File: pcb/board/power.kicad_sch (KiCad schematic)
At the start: 21 parts, among them Q1 DMG2305UX, U2 BQ25172, U3 TLV61070A, U4 XC6206P332MR

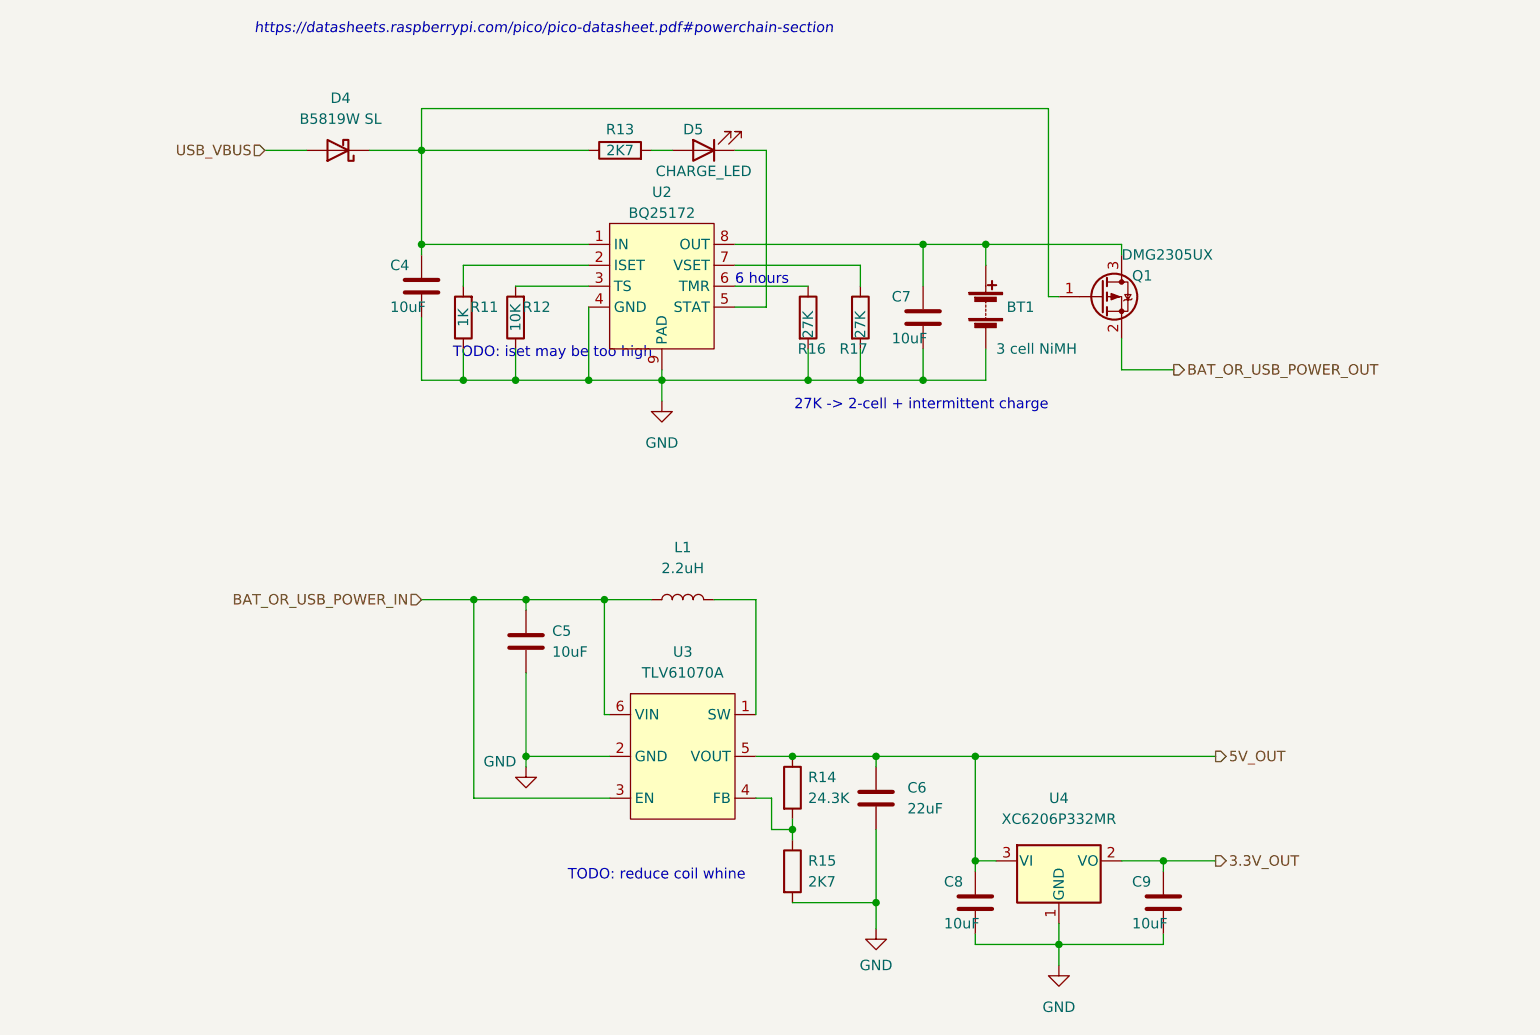
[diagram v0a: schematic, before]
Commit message: Update readmes. Uncovered I2C bug :(
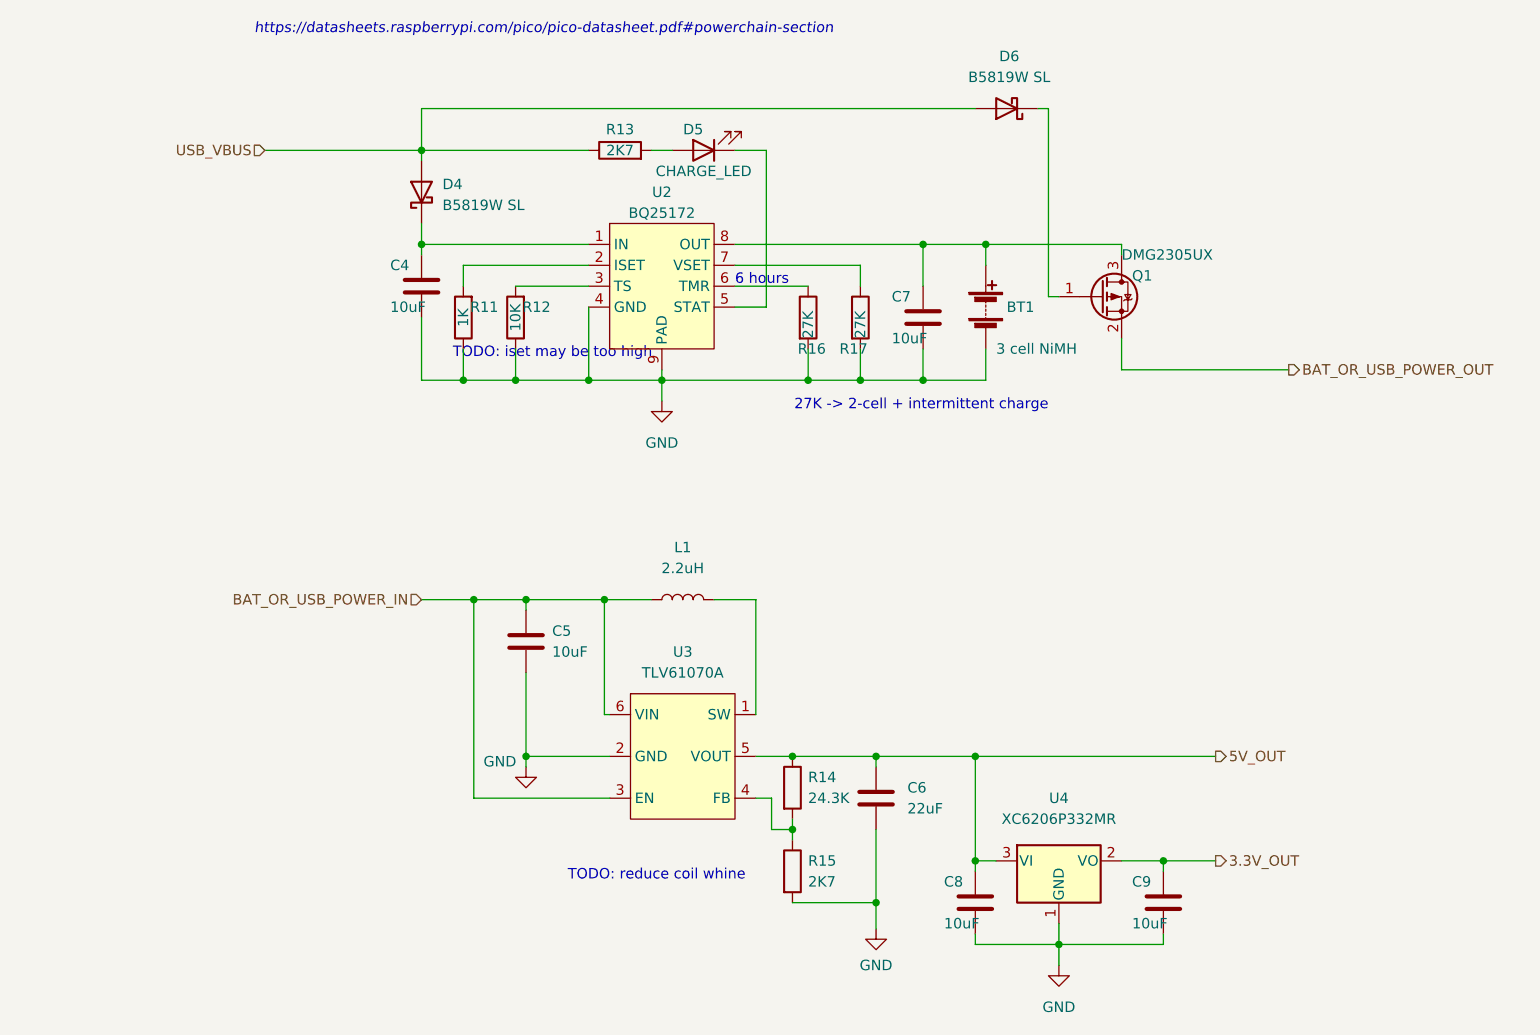
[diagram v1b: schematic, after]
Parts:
- added D6: B5819W SL, Diode_SMD:D_SOD-123, symbol Diode:1N5819
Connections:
- net USB_VBUS: now also R13.1, D6.2 (A)
- net at C4.1, D4.1 (K), U2.1 (IN): no longer Q1.1 (G), R13.1
- new net: D6.1 (K), Q1.1 (G)
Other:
- moved on the sheet: D4
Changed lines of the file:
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@@
+    (stroke (width 0) (type default) (color 0 0 0 0))
+  )
+  (wire (pts (xy 88.9 45.72) (xy 107.95 45.72))
     (stroke (width 0) (type default) (color 0 0 0 0))
   )
@@
     (stroke (width 0) (type default) (color 0 0 0 0))
   )
-  (wire (pts (xy 107.95 40.64) (xy 184.15 40.64))
+  (wire (pts (xy 107.95 40.64) (xy 175.26 40.64))
     (stroke (width 0) (type default) (color 0 0 0 0))
   )
@@
     (stroke (width 0) (type default) (color 0 0 0 0))
   )
-  (wire (pts (xy 107.95 45.72) (xy 107.95 57.15))
+  (wire (pts (xy 107.95 45.72) (xy 107.95 46.99))
     (stroke (width 0) (type default) (color 0 0 0 0))
   )
@@
     (stroke (width 0) (type default) (color 0 0 0 0))
   )
+  (wire (pts (xy 107.95 54.61) (xy 107.95 57.15))
+    (stroke (width 0) (type default) (color 0 0 0 0))
+  )
   (wire (pts (xy 168.91 73.66) (xy 161.29 73.66))
     (stroke (width 0) (type default) (color 0 0 0 0))
   )
-  (wire (pts (xy 193.04 72.39) (xy 199.39 72.39))
+  (wire (pts (xy 193.04 72.39) (xy 213.36 72.39))
     (stroke (width 0) (type default) (color 0 0 0 0))
   )
@@
     (stroke (width 0) (type default) (color 0 0 0 0))
   )
-  (wire (pts (xy 101.6 45.72) (xy 107.95 45.72))
-    (stroke (width 0) (type default) (color 0 0 0 0))
-  )
-  (wire (pts (xy 88.9 45.72) (xy 93.98 45.72))
-    (stroke (width 0) (type default) (color 0 0 0 0))
-  )
   (wire (pts (xy 163.195 137.16) (xy 163.195 140.335))
     (stroke (width 0) (type default) (color 0 0 0 0))
@@
   )
   (wire (pts (xy 163.195 119.38) (xy 163.195 120.65))
+    (stroke (width 0) (type default) (color 0 0 0 0))
+  )
+  (wire (pts (xy 182.88 40.64) (xy 184.15 40.64))
     (stroke (width 0) (type default) (color 0 0 0 0))
   )
@@
     (effects (font (size 1.27 1.27)) (justify right))
   )
-  (hierarchical_label "BAT_OR_USB_POWER_OUT" (shape output) (at 199.39 72.39 0)
+  (hierarchical_label "BAT_OR_USB_POWER_OUT" (shape output) (at 213.36 72.39 0)
     (effects (font (size 1.27 1.27)) (justify left))
   )
@@
     (pin "2")
   )
-  (symbol (lib_id "Diode:1N5819") (at 97.79 45.72 180) (unit 1)
-    (in_bom yes) (on_board yes) (fields_autoplaced)
-    (property "Reference" "D4" (id 0) (at 98.1075 39.37 0))
-    (property "Value" "B5819W SL" (id 1) (at 98.1075 41.91 0))
-    (property "Footprint" "Diode_SMD:D_SOD-123" (id 2) (at 97.79 41.275 0)
-      (effects (font (size 1.27 1.27)) hide)
-    )
-    (property "Datasheet" "" (id 3) (at 97.79 45.72 0)
-      (effects (font (size 1.27 1.27)) hide)
-    )
-    (property "Vendor" "C8598" (id 4) (at 97.79 45.72 0)
-      (effects (font (size 1.27 1.27)) hide)
-    )
+  (symbol (lib_id "Diode:1N5819") (at 179.07 40.64 180) (unit 1)
+    (in_bom yes) (on_board yes) (fields_autoplaced)
+    (property "Reference" "D6" (id 0) (at 179.3875 34.29 0))
+    (property "Value" "B5819W SL" (id 1) (at 179.3875 36.83 0))
+    (property "Footprint" "Diode_SMD:D_SOD-123" (id 2) (at 179.07 36.195 0)
+      (effects (font (size 1.27 1.27)) hide)
+    )
+    (property "Datasheet" "" (id 3) (at 179.07 40.64 0)
+      (effects (font (size 1.27 1.27)) hide)
+    )
+    (property "Vendor" "C8598" (id 4) (at 179.07 40.64 0)
+      (effects (font (size 1.27 1.27)) hide)
+    )
+    (pin "1")
+    (pin "2")
+  )
+  (symbol (lib_id "Diode:1N5819") (at 107.95 50.8 90) (unit 1)
+    (in_bom yes) (on_board yes) (fields_autoplaced)
+    (property "Reference" "D4" (id 0) (at 110.49 49.8474 90)
+      (effects (font (size 1.27 1.27)) (justify right))
+    )
+    (property "Value" "B5819W SL" (id 1) (at 110.49 52.3874 90)
+      (effects (font (size 1.27 1.27)) (justify right))
+    )
+    (property "Footprint" "Diode_SMD:D_SOD-123" (id 2) (at 112.395 50.8 0)
+      (effects (font (size 1.27 1.27)) hide)
+    )
+    (property "Datasheet" "" (id 3) (at 107.95 50.8 0)
+      (effects (font (size 1.27 1.27)) hide)
+    )
+    (property "Vendor" "C8598" (id 4) (at 107.95 50.8 0)
+      (effects (font (size 1.27 1.27)) hide)
+    )

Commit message: Update readme and pcb
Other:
- moved on the sheet: D6
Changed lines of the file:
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@@
     (stroke (width 0) (type default) (color 0 0 0 0))
   )
-  (wire (pts (xy 107.95 40.64) (xy 175.26 40.64))
+  (wire (pts (xy 107.95 40.64) (xy 109.22 40.64))
     (stroke (width 0) (type default) (color 0 0 0 0))
   )
@@
     (stroke (width 0) (type default) (color 0 0 0 0))
   )
-  (wire (pts (xy 182.88 40.64) (xy 184.15 40.64))
+  (wire (pts (xy 116.84 40.64) (xy 184.15 40.64))
     (stroke (width 0) (type default) (color 0 0 0 0))
   )
@@
     (pin "2")
   )
-  (symbol (lib_id "Diode:1N5819") (at 179.07 40.64 180) (unit 1)
-    (in_bom yes) (on_board yes) (fields_autoplaced)
-    (property "Reference" "D6" (id 0) (at 179.3875 34.29 0))
-    (property "Value" "B5819W SL" (id 1) (at 179.3875 36.83 0))
-    (property "Footprint" "Diode_SMD:D_SOD-123" (id 2) (at 179.07 36.195 0)
-      (effects (font (size 1.27 1.27)) hide)
-    )
-    (property "Datasheet" "" (id 3) (at 179.07 40.64 0)
-      (effects (font (size 1.27 1.27)) hide)
-    )
-    (property "Vendor" "C8598" (id 4) (at 179.07 40.64 0)
-      (effects (font (size 1.27 1.27)) hide)
-    )
+  (symbol (lib_id "Diode:1N5819") (at 113.03 40.64 180) (unit 1)
+    (in_bom yes) (on_board yes) (fields_autoplaced)
+    (property "Reference" "D6" (id 0) (at 113.3475 34.29 0))
+    (property "Value" "B5819W SL" (id 1) (at 113.3475 36.83 0))
+    (property "Footprint" "Diode_SMD:D_SOD-123" (id 2) (at 113.03 36.195 0)
+      (effects (font (size 1.27 1.27)) hide)
+    )
+    (property "Datasheet" "" (id 3) (at 113.03 40.64 0)
+      (effects (font (size 1.27 1.27)) hide)
+    )
+    (property "Vendor" "C8598" (id 4) (at 113.03 40.64 0)
+      (effects (font (size 1.27 1.27)) hide)
+    )

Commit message: update pcb
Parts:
- added JP1: CHG_LED_EN, Jumper:SolderJumper-2_P1.3mm_Bridged_RoundedPad1.0x1.5mm, symbol Jumper:Jumper_2_Bridged
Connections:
- net USB_VBUS: now also D5.2 (A); no longer R13.1
- net at D5.1 (K): now also JP1.1 (A); no longer U2.5 (STAT)
- net at R13.2: now also U2.5 (STAT); no longer D5.2 (A)
- new net: JP1.2 (B), R13.1
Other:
- moved on the sheet: D5, R13
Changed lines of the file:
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@@
+    (stroke (width 0) (type default) (color 0 0 0 0))
+  )
+  (wire (pts (xy 149.86 45.72) (xy 149.86 64.77))
     (stroke (width 0) (type default) (color 0 0 0 0))
   )
@@
     (stroke (width 0) (type default) (color 0 0 0 0))
   )
+  (wire (pts (xy 124.46 45.72) (xy 128.27 45.72))
+    (stroke (width 0) (type default) (color 0 0 0 0))
+  )
   (wire (pts (xy 148.59 119.38) (xy 153.035 119.38))
     (stroke (width 0) (type default) (color 0 0 0 0))
@@
     (stroke (width 0) (type default) (color 0 0 0 0))
   )
-  (wire (pts (xy 107.95 45.72) (xy 128.27 45.72))
+  (wire (pts (xy 107.95 45.72) (xy 116.84 45.72))
     (stroke (width 0) (type default) (color 0 0 0 0))
   )
@@
     (stroke (width 0) (type default) (color 0 0 0 0))
   )
+  (wire (pts (xy 140.97 45.72) (xy 138.43 45.72))
+    (stroke (width 0) (type default) (color 0 0 0 0))
+  )
   (wire (pts (xy 168.91 73.66) (xy 176.53 73.66))
     (stroke (width 0) (type default) (color 0 0 0 0))
@@
     (stroke (width 0) (type default) (color 0 0 0 0))
   )
-  (wire (pts (xy 149.86 64.77) (xy 149.86 45.72))
-    (stroke (width 0) (type default) (color 0 0 0 0))
-  )
   (wire (pts (xy 107.95 57.15) (xy 128.27 57.15))
     (stroke (width 0) (type default) (color 0 0 0 0))
@@
     (stroke (width 0) (type default) (color 0 0 0 0))
   )
+  (wire (pts (xy 161.29 69.85) (xy 161.29 73.66))
+    (stroke (width 0) (type default) (color 0 0 0 0))
+  )
   (wire (pts (xy 116.84 40.64) (xy 184.15 40.64))
     (stroke (width 0) (type default) (color 0 0 0 0))
   )
-  (wire (pts (xy 161.29 69.85) (xy 161.29 73.66))
-    (stroke (width 0) (type default) (color 0 0 0 0))
-  )
   (wire (pts (xy 153.035 137.16) (xy 163.195 137.16))
     (stroke (width 0) (type default) (color 0 0 0 0))
@@
     (stroke (width 0) (type default) (color 0 0 0 0))
   )
+  (wire (pts (xy 148.59 45.72) (xy 149.86 45.72))
+    (stroke (width 0) (type default) (color 0 0 0 0))
+  )
   (wire (pts (xy 176.53 69.85) (xy 176.53 73.66))
     (stroke (width 0) (type default) (color 0 0 0 0))
@@
     (stroke (width 0) (type default) (color 0 0 0 0))
   )
-  (wire (pts (xy 149.86 45.72) (xy 146.05 45.72))
-    (stroke (width 0) (type default) (color 0 0 0 0))
-  )
-  (wire (pts (xy 135.89 45.72) (xy 138.43 45.72))
-    (stroke (width 0) (type default) (color 0 0 0 0))
-  )
   (wire (pts (xy 153.035 119.38) (xy 163.195 119.38))
     (stroke (width 0) (type default) (color 0 0 0 0))
@@
     (stroke (width 0) (type default) (color 0 0 0 0))
   )
-  (text "TODO: iset may be too high\n" (at 111.76 71.12 0)
+  (text "TODO: iset may be too high\n" (at 107.95 76.2 0)
     (effects (font (size 1.27 1.27)) (justify left bottom))
   )
@@
     (pin "1")
   )
-  (symbol (lib_id "Device:LED") (at 142.24 45.72 180) (unit 1)
-    (in_bom yes) (on_board yes)
-    (property "Reference" "D5" (id 0) (at 140.97 43.18 0))
-    (property "Value" "CHARGE_LED" (id 1) (at 142.24 48.26 0))
-    (property "Footprint" "LED_SMD:LED_0805_2012Metric" (id 2) (at 142.24 45.72 0)
-      (effects (font (size 1.27 1.27)) hide)
-    )
-    (property "Datasheet" "~" (id 3) (at 142.24 45.72 0)
-      (effects (font (size 1.27 1.27)) hide)
-    )
-    (property "Vendor" "C84256" (id 4) (at 142.24 45.72 0)
-      (effects (font (size 1.27 1.27)) hide)
-    )
-    (pin "1")
-    (pin "2")
-  )
-  (symbol (lib_id "Device:R") (at 132.08 45.72 90) (unit 1)
-    (in_bom yes) (on_board yes)
-    (property "Reference" "R13" (id 0) (at 132.08 43.18 90))
-    (property "Value" "2K7" (id 1) (at 132.08 45.72 90))
-    (property "Footprint" "Resistor_SMD:R_0603_1608Metric" (id 2) (at 132.08 47.498 90)
-      (effects (font (size 1.27 1.27)) hide)
-    )
-    (property "Datasheet" "~" (id 3) (at 132.08 45.72 0)
-      (effects (font (size 1.27 1.27)) hide)
-    )
-    (property "Vendor" "C13167" (id 4) (at 132.08 45.72 0)
+  (symbol (lib_id "Device:LED") (at 120.65 45.72 180) (unit 1)
+    (in_bom yes) (on_board yes)
+    (property "Reference" "D5" (id 0) (at 119.38 43.18 0))
+    (property "Value" "CHARGE_LED" (id 1) (at 120.65 48.26 0))
+    (property "Footprint" "LED_SMD:LED_0805_2012Metric" (id 2) (at 120.65 45.72 0)
+      (effects (font (size 1.27 1.27)) hide)
+    )
+    (property "Datasheet" "~" (id 3) (at 120.65 45.72 0)
+      (effects (font (size 1.27 1.27)) hide)
+    )
+    (property "Vendor" "C84256" (id 4) (at 120.65 45.72 0)
+      (effects (font (size 1.27 1.27)) hide)
+    )
+    (pin "1")
+    (pin "2")
+  )
+  (symbol (lib_id "Device:R") (at 144.78 45.72 90) (unit 1)
+    (in_bom yes) (on_board yes)
+    (property "Reference" "R13" (id 0) (at 144.78 43.18 90))
+    (property "Value" "2K7" (id 1) (at 144.78 45.72 90))
+    (property "Footprint" "Resistor_SMD:R_0603_1608Metric" (id 2) (at 144.78 47.498 90)
+      (effects (font (size 1.27 1.27)) hide)
+    )
+    (property "Datasheet" "~" (id 3) (at 144.78 45.72 0)
+      (effects (font (size 1.27 1.27)) hide)
+    )
+    (property "Vendor" "C13167" (id 4) (at 144.78 45.72 0)
       (effects (font (size 1.27 1.27)) hide)
     )
@@
       (effects (font (size 1.27 1.27)) hide)
     )
+    (pin "1")
+    (pin "2")
+  )
+  (symbol (lib_id "Jumper:Jumper_2_Bridged") (at 133.35 45.72 0) (unit 1)
+    (in_bom yes) (on_board yes)
+    (property "Reference" "JP1" (id 0) (at 133.35 46.99 0))
+    (property "Value" "CHG_LED_EN" (id 1) (at 133.35 43.18 0))
+    (property "Footprint" "Jumper:SolderJumper-2_P1.3mm_Bridged_RoundedPad1.0x1.5mm" (id 2) (at 133.35 45.72 0)
+      (effects (font (size 1.27 1.27)) hide)
+    )
+    (property "Datasheet" "~" (id 3) (at 133.35 45.72 0)
+      (effects (font (size 1.27 1.27)) hide)
+    )

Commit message: pcb version 0.3
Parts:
- added JP2: CHARGE_CTRL, Jumper:SolderJumper-2_P1.3mm_Bridged_RoundedPad1.0x1.5mm, symbol Jumper:Jumper_2_Bridged
- added JP3: V_SENSE_EN, Jumper:SolderJumper-2_P1.3mm_Bridged_RoundedPad1.0x1.5mm, symbol Jumper:Jumper_2_Bridged
- added Q2: AO3400A, Package_TO_SOT_SMD:SOT-23, symbol Transistor_FET:AO3400A
- added R21: 10K, Resistor_SMD:R_0603_1608Metric, symbol Device:R
- added R22, R23: 27K, Resistor_SMD:R_0603_1608Metric, symbol Device:R
- added SW1: PWR, Button_Switch_THT:SW_E-Switch_EG1224_SPDT_Angled, symbol Switch:SW_SPST
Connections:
- net BAT_OR_USB_POWER_IN: now also SW1.2 (B); no longer U3.3 (EN)
- net GND: now also Q2.2 (S), R21.1, R23.2
- net at BT1.1 (+), C7.1, Q1.3 (D)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: now also JP3.1 (A)
- net at R12.2, U2.3 (TS): now also JP2.2 (B)
- new net: JP2.1 (A), Q2.3 (D)
- new net: R23.1, SW1.1 (A), U3.3 (EN)
- new net: JP3.2 (B), R22.2
- new net BAT_V_SENSE: R22.1
- new net CHG_EN: Q2.1 (G), R21.2
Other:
- moved on the sheet: C4, C5, C6, C8, C9, D4, D6, L1, R11, R12, R14, R15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
